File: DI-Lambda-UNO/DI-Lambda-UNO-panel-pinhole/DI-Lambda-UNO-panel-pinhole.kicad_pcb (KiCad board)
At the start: 2 copper layers, 33.2 x 26.6 mm, 1 part

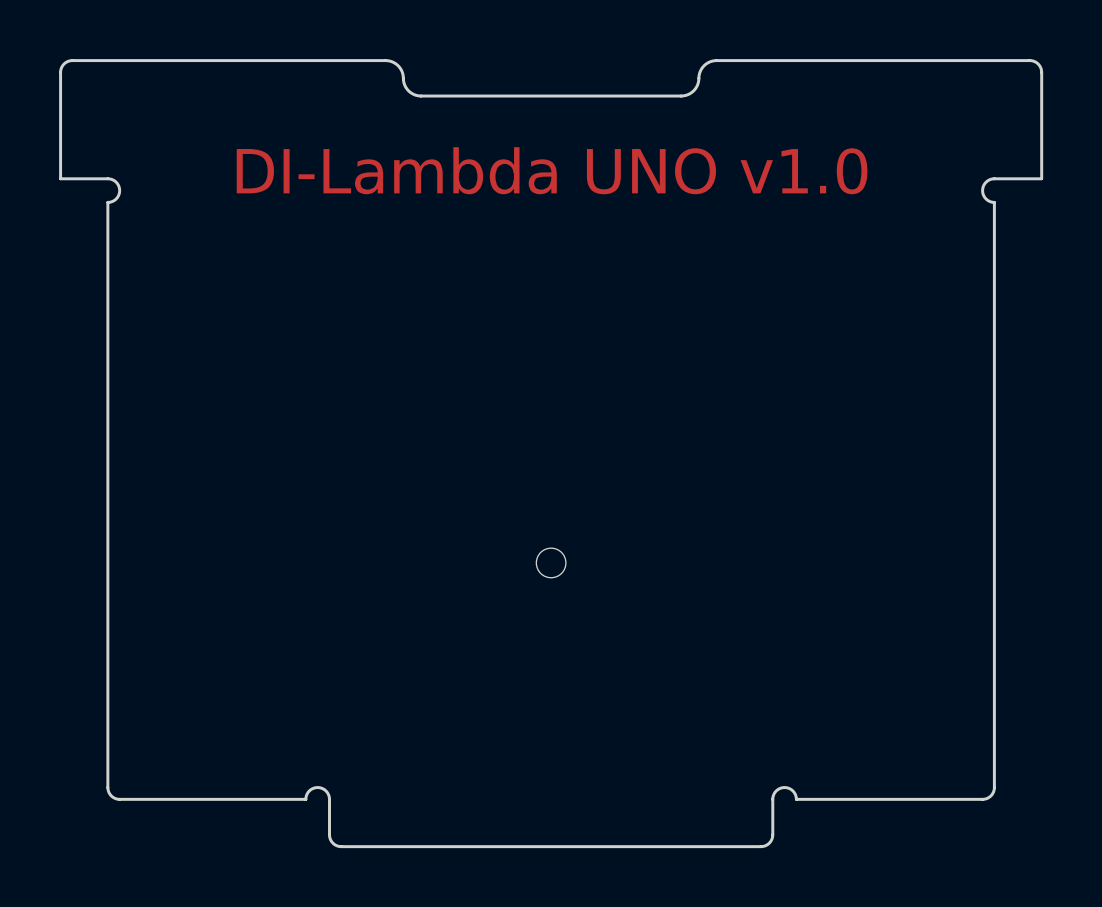
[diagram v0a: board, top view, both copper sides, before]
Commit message: Remove notches from the LED/Sensor/Pinhole panels
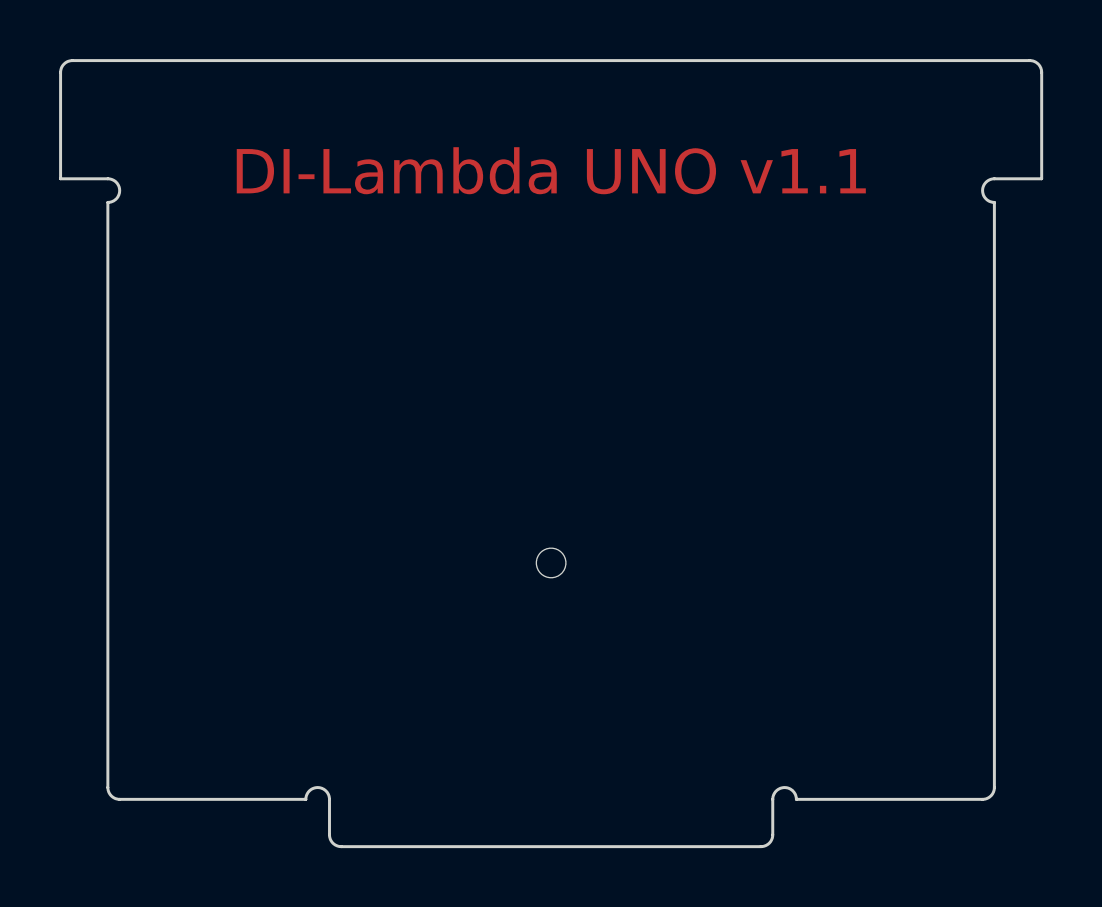
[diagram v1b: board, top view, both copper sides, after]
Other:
- outline, holes or cut-outs redrawn
- board text added: "DI-Lambda UNO v1.1"
- board text removed: "DI-Lambda UNO v1.0"
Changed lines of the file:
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@@
-(kicad_pcb (version 20170123) (host pcbnew "(2017-07-27 revision 3ee2f80)-test1")
+(kicad_pcb (version 20170123) (host pcbnew "(2017-09-07 revision 3b08636)-master")
   (general
     (thickness 1.6)
-    (drawings 32)
+    (drawings 26)
     (tracks 0)
     (zones 0)
@@
       (layerselection 0x000c0_7fffffff)
       (usegerberextensions true)
+      (usegerberattributes true)
+      (usegerberadvancedattributes true)
+      (creategerberjobfile true)
       (excludeedgelayer false)
       (linewidth 0.100000)
@@
     (pad "" np_thru_hole circle (at 0 0) (size 1 1) (drill 1) (layers *.Cu *.Mask))
   )
-  (gr_text "DI-Lambda UNO v1.0" (at 160 70.8) (layer F.Cu)
+  (gr_text "DI-Lambda UNO v1.1" (at 160 70.8) (layer F.Cu)
     (effects (font (size 1.5 1.5) (thickness 0.3)))
   )
@@
   (gr_arc (start 167.9 92) (end 167.5 92) (angle 180) (layer Edge.Cuts) (width 0.1))
   (gr_arc (start 152.1 92) (end 151.7 92) (angle 180) (layer Edge.Cuts) (width 0.1))
-  (gr_arc (start 164.4 67.6) (end 165 67.6) (angle 90) (layer Edge.Cuts) (width 0.1))
-  (gr_arc (start 165.6 67.6) (end 165 67.6) (angle 90) (layer Edge.Cuts) (width 0.1))
-  (gr_arc (start 154.4 67.6) (end 154.4 67) (angle 90) (layer Edge.Cuts) (width 0.1))
-  (gr_arc (start 155.6 67.6) (end 155.6 68.2) (angle 90) (layer Edge.Cuts) (width 0.1))
   (gr_line (start 175 91.6) (end 175 71.8) (layer Edge.Cuts) (width 0.1))
-  (gr_line (start 154.4 67) (end 143.8 67) (layer Edge.Cuts) (width 0.1))
+  (gr_line (start 176.2 67) (end 143.8 67) (layer Edge.Cuts) (width 0.1))
   (gr_line (start 175 71) (end 176.6 71) (layer Edge.Cuts) (width 0.1))
   (gr_line (start 145 91.6) (end 145 71.8) (layer Edge.Cuts) (width 0.1))
@@
   (gr_line (start 152.5 92) (end 152.5 93.2) (layer Edge.Cuts) (width 0.1))
   (gr_line (start 145.4 92) (end 151.7 92) (layer Edge.Cuts) (width 0.1))
-  (gr_line (start 176.2 67) (end 165.6 67) (layer Edge.Cuts) (width 0.1))
-  (gr_line (start 155.6 68.2) (end 164.4 68.2) (layer Edge.Cuts) (width 0.1))
 )
